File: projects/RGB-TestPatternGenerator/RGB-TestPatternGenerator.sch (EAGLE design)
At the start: 15 parts, among them IC1 7805TV, IC2 7809TV, IC3 4060N, IC4 4040N, IC5 74HC10N, IC6 4082N, IC7 74HC32N, IC8 74LS157N

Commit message: feat: rgb schematic
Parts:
- added C10, C11, C12, C13, C8, C9: 100nF, rcl:C-EU050-024X044
- added C6, C7: 10pF, rcl:C-EU050-024X044
- added JP1: (no value), jumper:JP2E
- added JP2: (no value), jumper:JP1E
- added R1: 1M, rcl:R-EU_0207/10
- added R10, R14, R15, R16, R8, R9: 120R, rcl:R-EU_0207/10
- added R11: 100R, rcl:R-EU_0207/10
- added R12, R13: 47R, rcl:R-EU_0207/10
- added R17, R18, R19: 68R, rcl:R-EU_0207/10
- added R2, R4, R6, R7: 1k, rcl:R-EU_0207/10
- added R3: 2.2k, rcl:R-EU_0207/10
- added R5: 3.9k, rcl:R-EU_0207/10
- added X1: D-SUB15-HDR15RA, con-thomas-betts:D-SUB15-HDR15RA
- added Y1: 8MHz, SparkFun-Clocks:CRYSTALPTH-HC49US
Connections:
- new net N$10: IC5C.O, IC8A.1A, IC8A.2A, IC8A.3A
- new net N$11: IC7C.O, IC8A.G
- new net N$12: IC4A.Q6, IC5B.I2, IC6A.I2
- new net N$13: IC4A.Q5, IC5B.I1
- new net N$14: IC4A.Q1, IC5B.I0
- new net N$15: IC4A.Q7, IC6A.I0
- new net N$16: IC4A.Q8, IC6A.I1
- new net N$17: IC5A.O, IC5C.I2
- new net N$18: IC4A.Q9, IC6A.I3
- new net N$19: IC5B.O, IC5C.I0
- new net N$2: C6.1, IC3A.P1, R1.1, Y1.1
- new net N$20: IC6A.O, IC7A.I0, IC7A.I1, IC7D.I1
- new net N$21: IC8A.1Y, R2.1, R3.1
- new net N$22: IC6B.O, IC7B.I0, IC7B.I1, IC7D.I0
- new net N$23: IC8A.2Y, R4.1, R5.1
- new net N$24: IC8A.3Y, R6.1, R7.1
- new net N$25: C11.1, C12.1, C13.1, R11.2, R3.2, R5.2, R7.2
- new net N$26: C9.1, R6.2, R8.2
- new net N$27: C10.1, R2.2, R9.2
- new net N$28: C8.1, R10.2, R4.2
- new net N$29: IC7C.I1, IC7D.O
- new net N$3: C7.1, IC3A.!P0, R1.2, Y1.2
- new net N$30: IC7B.O, R13.1
- new net N$31: IC7A.O, R12.1
- new net N$32: IC7C.I0, JP2.1, R14.1
- new net N$33: IC8A.!A!/B, JP1.3, R16.1
- new net N$34: R13.2, X1-13.F
- new net N$35: R12.2, X1-14.F
- new net N$36: R17.2, X1-1.F
- new net N$37: JP1.1, R15.1
- new net N$38: R18.2, X1-2.F
- new net N$39: R19.2, X1-3.F
- new net N$4: IC3A.Q5, IC5A.I1, IC6B.I2
- new net N$5: IC3A.Q6, IC6B.I3, IC8A.2B
- new net N$6: IC3A.Q4, IC5A.I0
- new net N$7: IC3A.P0, IC5A.I2
- new net N$8: IC3A.Q7, IC6B.I1, IC8A.1B
- new net N$9: IC3A.Q8, IC4A.P1, IC6B.I0, IC8A.3B
- net GND: now also C6.2, C7.2, IC3A.RES, IC4A.RES, JP1.2, JP2.2, R10.1, R11.1, R8.1, R9.1, X1-10.F, X1-5.F, X1-6.F, X1-7.F, X1-8.F
- net VCC: now also IC5C.I1, R14.2, R15.2, R16.2
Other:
- moved on the sheet: C1, C2, C3, C4, C5, GND, IC1, IC2, IC3, IC4, IC5A, IC5B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

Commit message: feat: rgb schematic
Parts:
- added U$1: TEA5114A, bb84:RGBTEA5114A
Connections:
- new net N$40: R17.1, U$1.R
- new net N$41: R18.1, U$1.G
- new net N$42: R19.1, U$1.B
- new net N$43: C13.2, U$1.R1
- new net N$44: C10.2, U$1.R2
- new net N$45: C12.2, U$1.G1
- new net N$46: C9.2, U$1.G2
- new net N$47: C11.2, U$1.B1
- new net N$48: C8.2, U$1.B2
- new net N$49: U$1.FBB, U$1.FBG, U$1.FBR
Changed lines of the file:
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@@
 <setting verticaltext="up"/>
 </settings>
-<grid distance="0.1" unitdist="inch" unit="inch" style="lines" multiple="1" display="yes" altdistance="0.01" altunitdist="inch" altunit="inch"/>
+<grid distance="0.1" unitdist="inch" unit="inch" style="lines" multiple="1" display="no" altdistance="0.01" altunitdist="inch" altunit="inch"/>
 <layers>
 <layer number="1" name="Top" color="4" fill="1" visible="no" active="no"/>
@@
 <part name="R18" library="rcl" library_urn="urn:adsk.eagle:library:334" deviceset="R-EU_" device="0207/10" package3d_urn="urn:adsk.eagle:package:23491/2" value="68R"/>
 <part name="R19" library="rcl" library_urn="urn:adsk.eagle:library:334" deviceset="R-EU_" device="0207/10" package3d_urn="urn:adsk.eagle:package:23491/2" value="68R"/>
+<part name="U$1" library="bb84" deviceset="RGB" device="TEA5114A" package3d_urn="urn:adsk.eagle:package:43556886/1" value="TEA5114A"/>
 </parts>
 <sheets>
@@
 <attribute name="NAME" x="196.85" y="98.0186" size="1.778" layer="95"/>
 <attribute name="VALUE" x="196.85" y="93.218" size="1.778" layer="96"/>
+</instance>
+<instance part="U$1" gate="G$1" x="200.66" y="12.7" smashed="yes">
+<attribute name="NAME" x="180.34" y="35.56" size="1.778" layer="95"/>
+<attribute name="VALUE" x="180.34" y="7.62" size="1.778" layer="96"/>
 </instance>
 </instances>
@@
 </segment>
 </net>
+<net name="N$40" class="0">
+<segment>
+<pinref part="U$1" gate="G$1" pin="R"/>
+<wire x1="198.12" y1="30.48" x2="200.66" y2="30.48" width="0.1524" layer="91"/>
+<wire x1="200.66" y1="30.48" x2="200.66" y2="35.56" width="0.1524" layer="91"/>
+<wire x1="200.66" y1="35.56" x2="175.26" y2="35.56" width="0.1524" layer="91"/>
+<pinref part="R17" gate="G$1" pin="1"/>
+<wire x1="175.26" y1="35.56" x2="175.26" y2="101.6" width="0.1524" layer="91"/>
+<wire x1="175.26" y1="101.6" x2="177.8" y2="101.6" width="0.1524" layer="91"/>
+</segment>
+</net>
+<net name="N$41" class="0">
+<segment>
+<pinref part="U$1" gate="G$1" pin="G"/>
+<wire x1="198.12" y1="22.86" x2="203.2" y2="22.86" width="0.1524" layer="91"/>
+<wire x1="203.2" y1="22.86" x2="203.2" y2="38.1" width="0.1524" layer="91"/>
+<wire x1="203.2" y1="38.1" x2="177.8" y2="38.1" width="0.1524" layer="91"/>
+<pinref part="R18" gate="G$1" pin="1"/>
+<wire x1="177.8" y1="38.1" x2="177.8" y2="99.06" width="0.1524" layer="91"/>
+<wire x1="177.8" y1="99.06" x2="185.42" y2="99.06" width="0.1524" layer="91"/>
+</segment>
+</net>
+<net name="N$42" class="0">
+<segment>
+<pinref part="U$1" gate="G$1" pin="B"/>
+<wire x1="198.12" y1="17.78" x2="205.74" y2="17.78" width="0.1524" layer="91"/>
+<wire x1="205.74" y1="17.78" x2="205.74" y2="40.64" width="0.1524" layer="91"/>
+<wire x1="205.74" y1="40.64" x2="180.34" y2="40.64" width="0.1524" layer="91"/>
+<pinref part="R19" gate="G$1" pin="1"/>
+<wire x1="180.34" y1="40.64" x2="180.34" y2="96.52" width="0.1524" layer="91"/>
+<wire x1="180.34" y1="96.52" x2="193.04" y2="96.52" width="0.1524" layer="91"/>
+</segment>
+</net>
+<net name="N$43" class="0">
+<segment>
+<pinref part="U$1" gate="G$1" pin="R1"/>
+<pinref part="C13" gate="G$1" pin="2"/>
+<wire x1="177.8" y1="30.48" x2="160.02" y2="30.48" width="0.1524" layer="91"/>
+</segment>
+</net>
+<net name="N$44" class="0">
+<segment>
+<pinref part="U$1" gate="G$1" pin="R2"/>
+<pinref part="C10" gate="G$1" pin="2"/>
+<wire x1="177.8" y1="25.4" x2="144.78" y2="25.4" width="0.1524" layer="91"/>
+</segment>
+</net>
+<net name="N$45" class="0">
+<segment>
+<pinref part="C12" gate="G$1" pin="2"/>
+<wire x1="160.02" y1="20.32" x2="162.56" y2="20.32" width="0.1524" layer="91"/>
+<wire x1="162.56" y1="20.32" x2="162.56" y2="22.86" width="0.1524" layer="91"/>
+<pinref part="U$1" gate="G$1" pin="G1"/>
+<wire x1="162.56" y1="22.86" x2="177.8" y2="22.86" width="0.1524" layer="91"/>
+</segment>
+</net>
+<net name="N$46" class="0">
+<segment>
+<pinref part="U$1" gate="G$1" pin="G2"/>
+<wire x1="177.8" y1="20.32" x2="165.1" y2="20.32" width="0.1524" layer="91"/>
+<wire x1="165.1" y1="20.32" x2="165.1" y2="15.24" width="0.1524" layer="91"/>
+<pinref part="C9" gate="G$1" pin="2"/>
+<wire x1="165.1" y1="15.24" x2="144.78" y2="15.24" width="0.1524" layer="91"/>
+</segment>
+</net>
+<net name="N$47" class="0">
+<segment>
+<pinref part="C11" gate="G$1" pin="2"/>
+<wire x1="160.02" y1="10.16" x2="167.64" y2="10.16" width="0.1524" layer="91"/>
+<pinref part="U$1" gate="G$1" pin="B1"/>
+<wire x1="167.64" y1="10.16" x2="167.64" y2="17.78" width="0.1524" layer="91"/>
+<wire x1="167.64" y1="17.78" x2="177.8" y2="17.78" width="0.1524" layer="91"/>
+</segment>
+</net>
+<net name="N$48" class="0">
+<segment>
+<pinref part="U$1" gate="G$1" pin="B2"/>
+<wire x1="177.8" y1="15.24" x2="170.18" y2="15.24" width="0.1524" layer="91"/>
+<wire x1="170.18" y1="15.24" x2="170.18" y2="5.08" width="0.1524" layer="91"/>
+<pinref part="C8" gate="G$1" pin="2"/>
+<wire x1="170.18" y1="5.08" x2="144.78" y2="5.08" width="0.1524" layer="91"/>
+</segment>
+</net>
+<net name="N$49" class="0">
+<segment>
+<pinref part="U$1" gate="G$1" pin="FBR"/>
+<wire x1="198.12" y1="27.94" x2="200.66" y2="27.94" width="0.1524" layer="91"/>
+<wire x1="200.66" y1="27.94" x2="200.66" y2="20.32" width="0.1524" layer="91"/>
+<pinref part="U$1" gate="G$1" pin="FBG"/>
+<wire x1="200.66" y1="20.32" x2="198.12" y2="20.32" width="0.1524" layer="91"/>
+<wire x1="200.66" y1="20.32" x2="200.66" y2="15.24" width="0.1524" layer="91"/>
+<junction x="200.66" y="20.32"/>
+<pinref part="U$1" gate="G$1" pin="FBB"/>
+<wire x1="200.66" y1="15.24" x2="198.12" y2="15.24" width="0.1524" layer="91"/>
+</segment>
+</net>

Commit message: feat: rgb schematic
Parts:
- added D1: 1N4148DO35-7, diode:1N4148DO35-7
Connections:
- net GND: now also U$1.GND
- net N$37: now also D1.A
- net N$49: now also D1.C
- net VCC: now also U$1.VCC
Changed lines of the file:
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@@
 <part name="R19" library="rcl" library_urn="urn:adsk.eagle:library:334" deviceset="R-EU_" device="0207/10" package3d_urn="urn:adsk.eagle:package:23491/2" value="68R"/>
 <part name="U$1" library="bb84" deviceset="RGB" device="TEA5114A" package3d_urn="urn:adsk.eagle:package:43556886/1" value="TEA5114A"/>
+<part name="P+8" library="supply1" library_urn="urn:adsk.eagle:library:371" deviceset="VCC" device="" value="+9V"/>
+<part name="D1" library="diode" library_urn="urn:adsk.eagle:library:210" deviceset="1N4148" device="DO35-7" package3d_urn="urn:adsk.eagle:package:43339/2"/>
+<part name="GND18" library="supply1" library_urn="urn:adsk.eagle:library:371" deviceset="GND" device=""/>
 </parts>
 <sheets>
@@
 <attribute name="VALUE" x="132.842" y="-8.89" size="1.778" layer="96" rot="R90"/>
 </instance>
-<instance part="GND12" gate="1" x="114.3" y="-15.24" smashed="yes">
-<attribute name="VALUE" x="111.76" y="-17.78" size="1.778" layer="96"/>
-</instance>
-<instance part="GND13" gate="1" x="121.92" y="-15.24" smashed="yes">
-<attribute name="VALUE" x="119.38" y="-17.78" size="1.778" layer="96"/>
-</instance>
-<instance part="GND14" gate="1" x="129.54" y="-15.24" smashed="yes">
-<attribute name="VALUE" x="127" y="-17.78" size="1.778" layer="96"/>
+<instance part="GND12" gate="1" x="114.3" y="-20.32" smashed="yes">
+<attribute name="VALUE" x="111.76" y="-22.86" size="1.778" layer="96"/>
+</instance>
+<instance part="GND13" gate="1" x="121.92" y="-20.32" smashed="yes">
+<attribute name="VALUE" x="119.38" y="-22.86" size="1.778" layer="96"/>
+</instance>
+<instance part="GND14" gate="1" x="129.54" y="-20.32" smashed="yes">
+<attribute name="VALUE" x="127" y="-22.86" size="1.778" layer="96"/>
 </instance>
 <instance part="C8" gate="G$1" x="139.7" y="5.08" smashed="yes" rot="R90">
@@
 <attribute name="VALUE" x="153.162" y="-8.89" size="1.778" layer="96" rot="R90"/>
 </instance>
-<instance part="GND15" gate="1" x="149.86" y="-15.24" smashed="yes">
-<attribute name="VALUE" x="147.32" y="-17.78" size="1.778" layer="96"/>
+<instance part="GND15" gate="1" x="149.86" y="-20.32" smashed="yes">
+<attribute name="VALUE" x="147.32" y="-22.86" size="1.778" layer="96"/>
 </instance>
 <instance part="R12" gate="G$1" x="147.32" y="78.74" smashed="yes">
@@
 <attribute name="VALUE" x="-7.62" y="-4.445" size="1.778" layer="96" rot="R180"/>
 </instance>
-<instance part="GND16" gate="1" x="-2.54" y="-15.24" smashed="yes">
-<attribute name="VALUE" x="-5.08" y="-17.78" size="1.778" layer="96"/>
+<instance part="GND16" gate="1" x="-2.54" y="-20.32" smashed="yes">
+<attribute name="VALUE" x="-5.08" y="-22.86" size="1.778" layer="96"/>
 </instance>
 <instance part="X1" gate="-1" x="208.28" y="101.6" smashed="yes">
@@
 <attribute name="NAME" x="180.34" y="35.56" size="1.778" layer="95"/>
 <attribute name="VALUE" x="180.34" y="7.62" size="1.778" layer="96"/>
+</instance>
+<instance part="P+8" gate="VCC" x="208.28" y="45.72" smashed="yes">
+<attribute name="VALUE" x="205.74" y="43.18" size="1.778" layer="96" rot="R90"/>
+</instance>
+<instance part="D1" gate="G$1" x="200.66" y="-5.08" smashed="yes" rot="R90">
+<attribute name="NAME" x="200.1774" y="-2.54" size="1.778" layer="95" rot="R90"/>
+<attribute name="VALUE" x="202.9714" y="-2.54" size="1.778" layer="96" rot="R90"/>
+</instance>
+<instance part="GND18" gate="1" x="175.26" y="5.08" smashed="yes">
+<attribute name="VALUE" x="172.72" y="2.54" size="1.778" layer="96"/>
 </instance>
 </instances>
@@
 <pinref part="R8" gate="G$1" pin="1"/>
 <pinref part="GND12" gate="1" pin="GND"/>
-<wire x1="114.3" y1="-10.16" x2="114.3" y2="-12.7" width="0.1524" layer="91"/>
+<wire x1="114.3" y1="-10.16" x2="114.3" y2="-17.78" width="0.1524" layer="91"/>
 </segment>
 <segment>
 <pinref part="R9" gate="G$1" pin="1"/>
 <pinref part="GND13" gate="1" pin="GND"/>
-<wire x1="121.92" y1="-10.16" x2="121.92" y2="-12.7" width="0.1524" layer="91"/>
+<wire x1="121.92" y1="-10.16" x2="121.92" y2="-17.78" width="0.1524" layer="91"/>
 </segment>
 <segment>
 <pinref part="R10" gate="G$1" pin="1"/>
 <pinref part="GND14" gate="1" pin="GND"/>
-<wire x1="129.54" y1="-10.16" x2="129.54" y2="-12.7" width="0.1524" layer="91"/>
+<wire x1="129.54" y1="-10.16" x2="129.54" y2="-17.78" width="0.1524" layer="91"/>
 </segment>
 <segment>
 <pinref part="R11" gate="G$1" pin="1"/>
 <pinref part="GND15" gate="1" pin="GND"/>
-<wire x1="149.86" y1="-10.16" x2="149.86" y2="-12.7" width="0.1524" layer="91"/>
+<wire x1="149.86" y1="-10.16" x2="149.86" y2="-17.78" width="0.1524" layer="91"/>
 </segment>
 <segment>
@@
 <wire x1="-2.54" y1="-7.62" x2="-5.08" y2="-7.62" width="0.1524" layer="91"/>
 <pinref part="GND16" gate="1" pin="GND"/>
-<wire x1="-2.54" y1="-12.7" x2="-2.54" y2="-7.62" width="0.1524" layer="91"/>
+<wire x1="-2.54" y1="-17.78" x2="-2.54" y2="-7.62" width="0.1524" layer="91"/>
 <junction x="-2.54" y="-7.62"/>
 </segment>
@@
 <junction x="200.66" y="88.9"/>
 </segment>
+<segment>
+<pinref part="U$1" gate="G$1" pin="GND"/>
+<wire x1="177.8" y1="27.94" x2="175.26" y2="27.94" width="0.1524" layer="91"/>
+<pinref part="GND18" gate="1" pin="GND"/>
+<wire x1="175.26" y1="27.94" x2="175.26" y2="7.62" width="0.1524" layer="91"/>
+</segment>
 </net>
 <net name="VCC" class="0">
@@
 <pinref part="IC5" gate="C" pin="I1"/>
 <wire x1="83.82" y1="78.74" x2="88.9" y2="78.74" width="0.1524" layer="91"/>
+</segment>
+<segment>
+<pinref part="P+8" gate="VCC" pin="VCC"/>
+<wire x1="208.28" y1="43.18" x2="208.28" y2="25.4" width="0.1524" layer="91"/>
+<pinref part="U$1" gate="G$1" pin="VCC"/>
+<wire x1="208.28" y1="25.4" x2="198.12" y2="25.4" width="0.1524" layer="91"/>
 </segment>
 </net>
@@
 <pinref part="R15" gate="G$1" pin="1"/>
 <wire x1="5.08" y1="-2.54" x2="5.08" y2="10.16" width="0.1524" layer="91"/>
+<pinref part="D1" gate="G$1" pin="A"/>
+<wire x1="200.66" y1="-7.62" x2="200.66" y2="-15.24" width="0.1524" layer="91"/>
+<wire x1="200.66" y1="-15.24" x2="5.08" y2="-15.24" width="0.1524" layer="91"/>
+<wire x1="5.08" y1="-15.24" x2="5.08" y2="-2.54" width="0.1524" layer="91"/>
+<junction x="5.08" y="-2.54"/>
 </segment>
 </net>
@@
 <pinref part="U$1" gate="G$1" pin="FBB"/>
 <wire x1="200.66" y1="15.24" x2="198.12" y2="15.24" width="0.1524" layer="91"/>
-</segment>
-</net>
+<pinref part="D1" gate="G$1" pin="C"/>
+<wire x1="200.66" y1="-2.54" x2="200.66" y2="15.24" width="0.1524" layer="91"/>
+<junction x="200.66" y="15.24"/>
+</segment>
+</net>

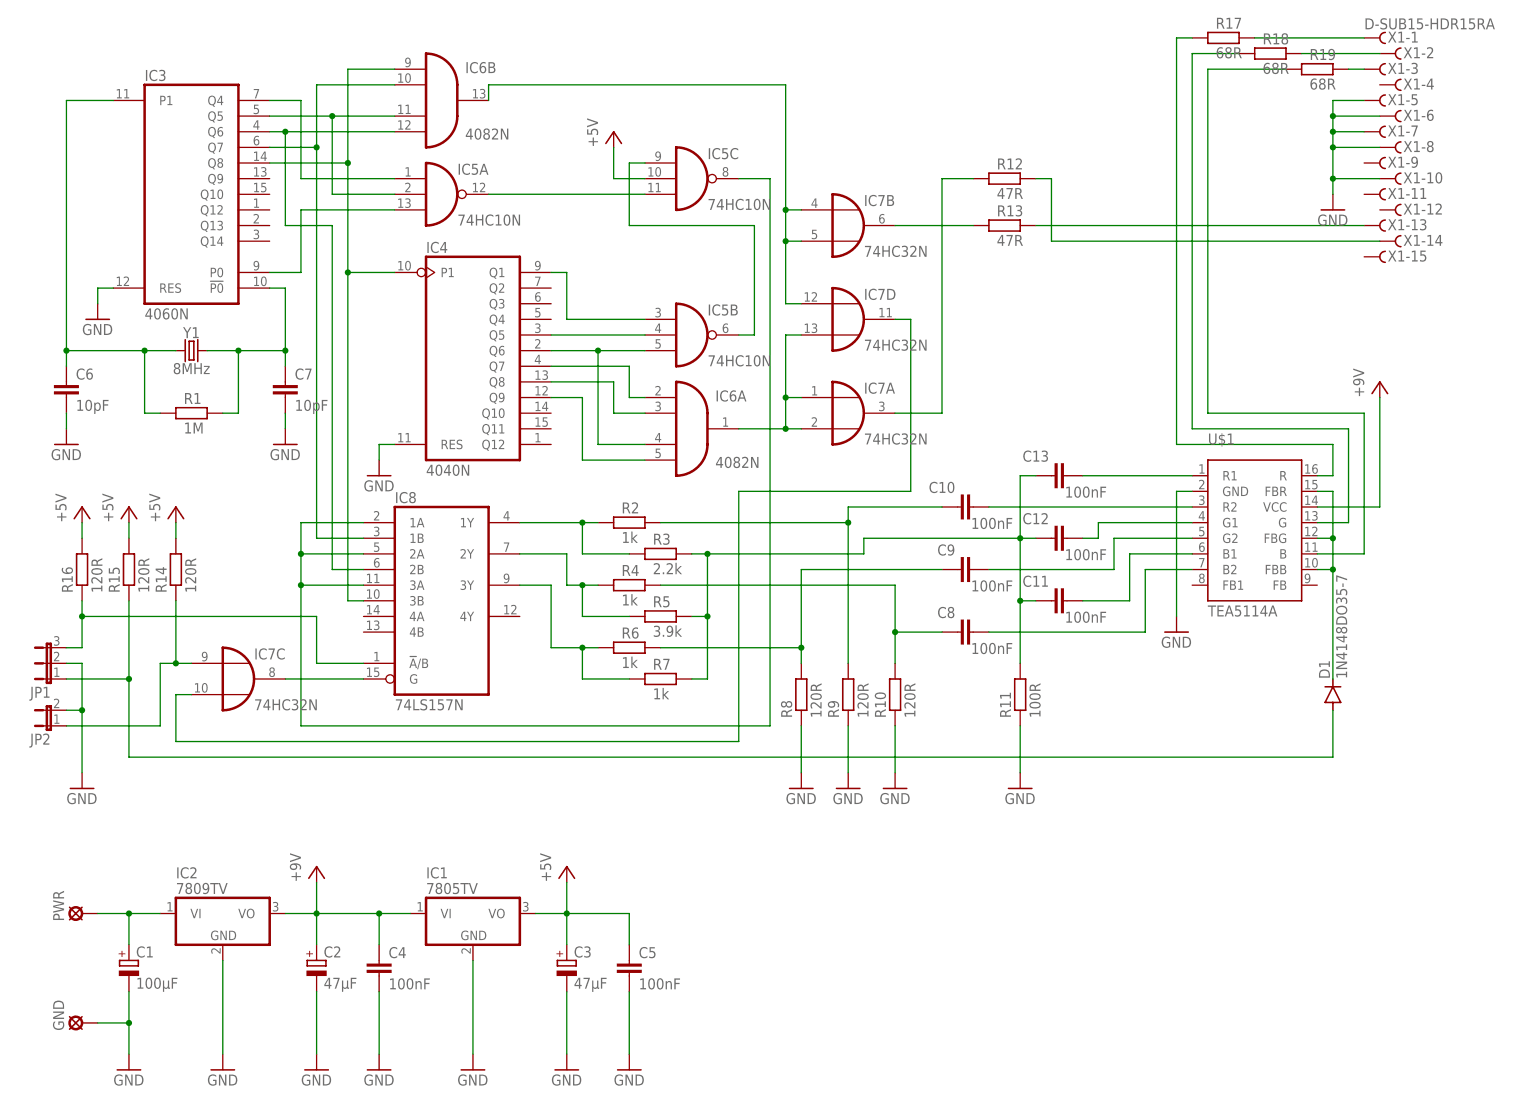
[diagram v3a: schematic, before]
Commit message: feat: rgb layout
chnages:
- schematic modified
- layout modified
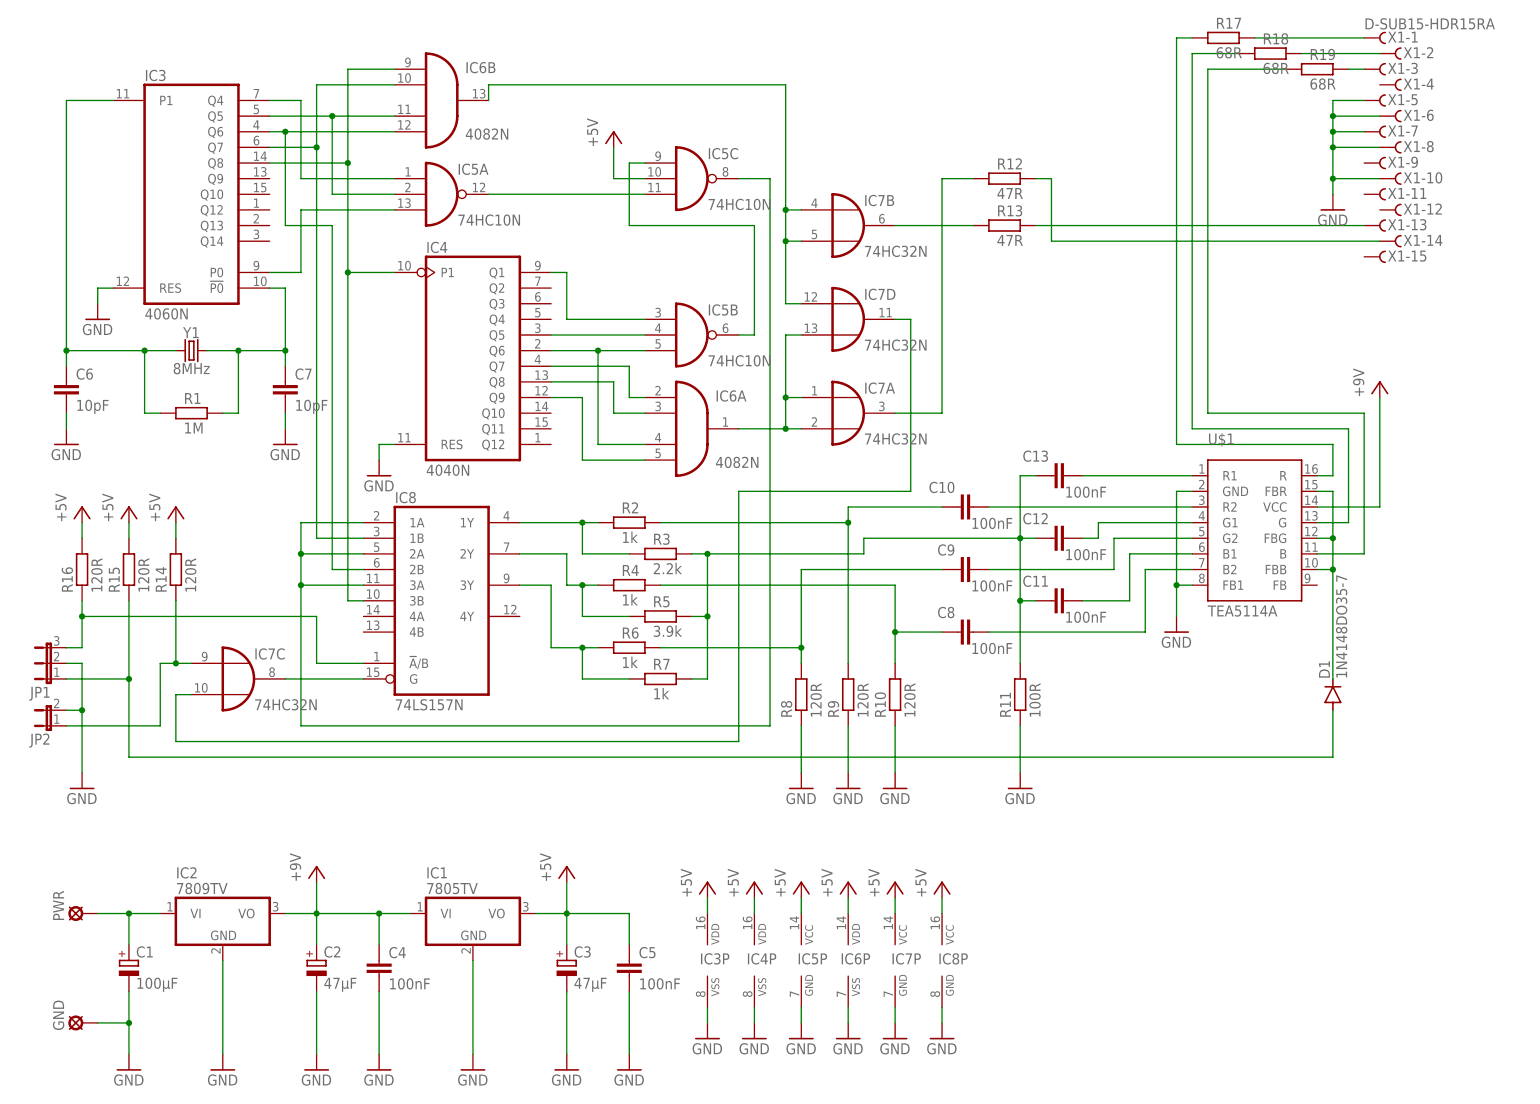
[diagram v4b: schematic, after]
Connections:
- new net +5V: C3.+, C5.1, IC1.VO, IC3P.VDD, IC4P.VDD, IC5C.I1, IC5P.VCC, IC6P.VDD, IC7P.VCC, IC8P.VCC, R14.2, R15.2, R16.2
- net GND: now also IC3P.VSS, IC4P.VSS, IC5P.GND, IC6P.VSS, IC7P.GND, IC8P.GND, U$1.FB1
- net VCC: no longer C3.+, C5.1, IC1.VO, IC5C.I1, R14.2, R15.2, R16.2
